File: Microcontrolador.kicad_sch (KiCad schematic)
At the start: 0 parts

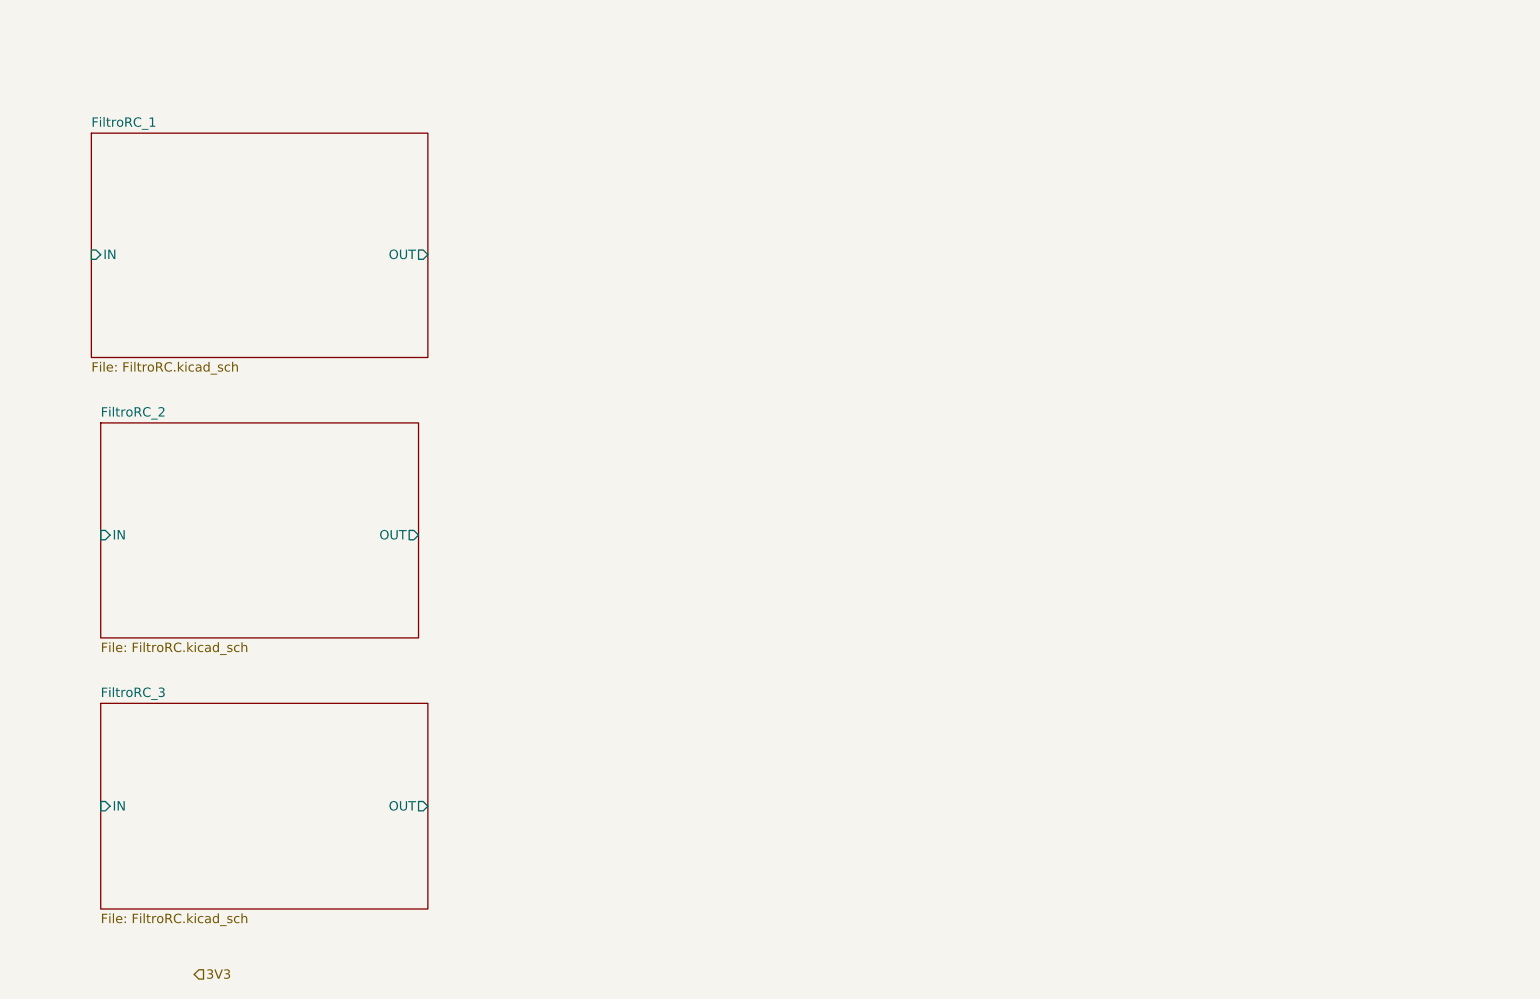
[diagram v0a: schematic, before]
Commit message: Microcontrolador: STM32G031K8T6, SWD, conector E/S y 3 filtros RC (huellas y MPN)
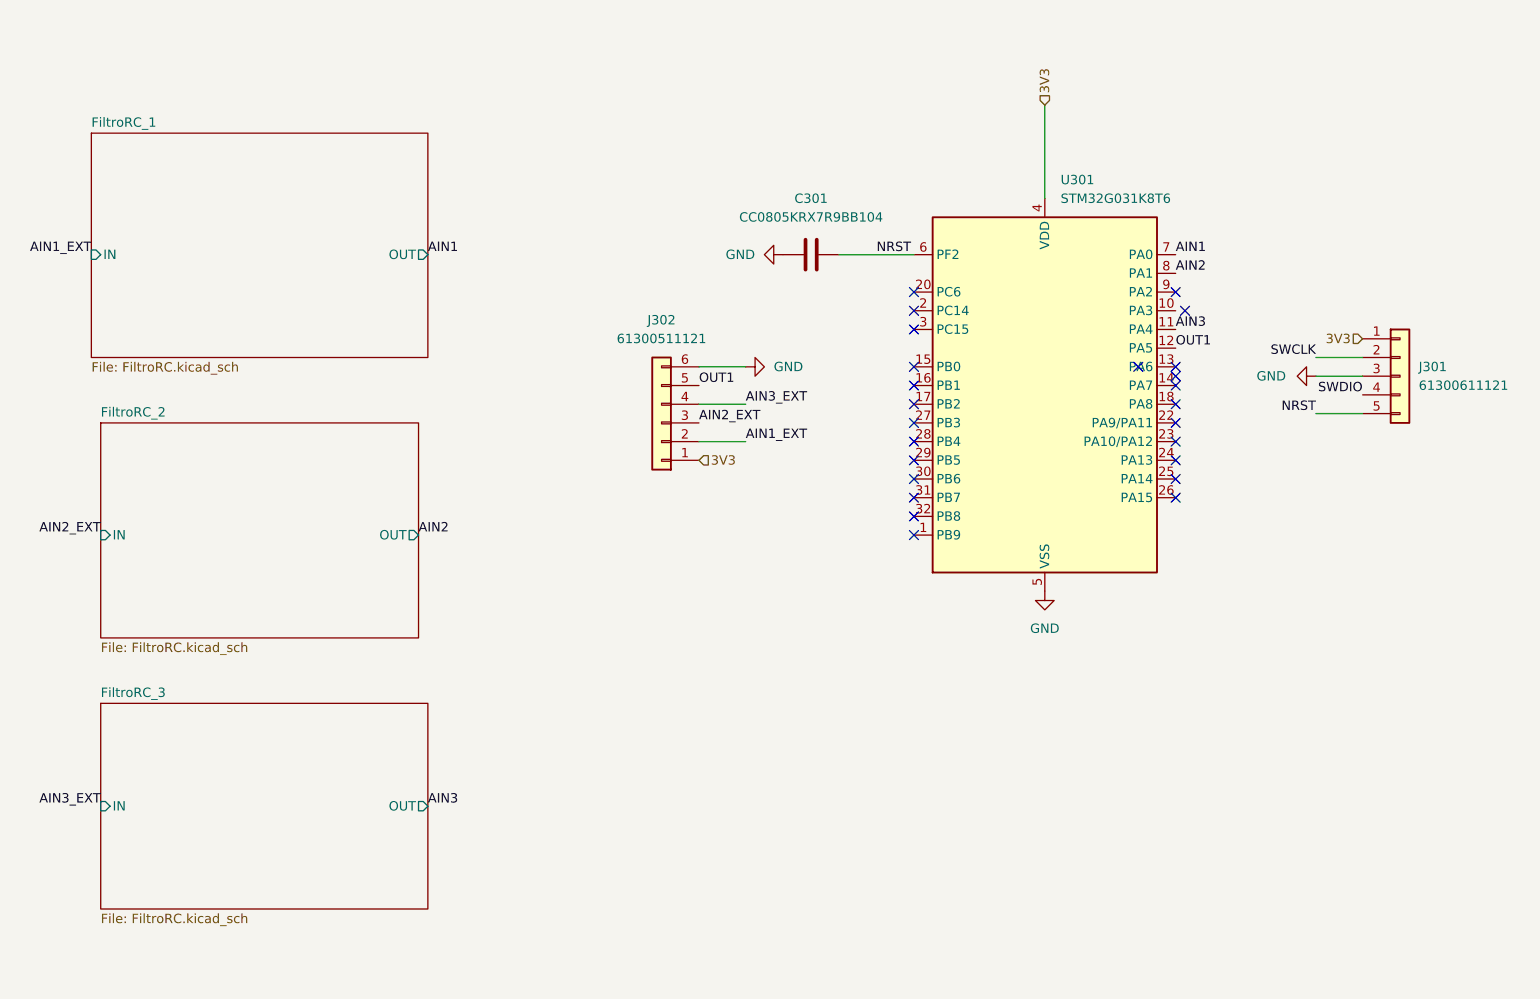
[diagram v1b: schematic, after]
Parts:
- added C301: CC0805KRX7R9BB104, Capacitor_SMD:C_0805_2012Metric_Pad1.18x1.45mm_HandSolder, symbol Device:C
- added J301: 61300611121, Connector_PinHeader_2.54mm:PinHeader_1x06_P2.54mm_Vertical, symbol Connector_Generic:Conn_01x05
- added J302: 61300511121, Connector_PinHeader_2.54mm:PinHeader_1x05_P2.54mm_Vertical, symbol Connector_Generic:Conn_01x06
- added U301: STM32G031K8T6, Package_QFP:LQFP-32_7x7mm_P0.8mm, symbol MCU_ST_STM32G0:STM32G031K8Tx
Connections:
- net 3V3: now also J301.1 (Pin_1), J302.1 (Pin_1), U301.4 (VDD)
- new net AIN1: U301.7 (PA0)
- new net AIN1_EXT: J302.2 (Pin_2)
- new net AIN2: U301.8 (PA1)
- new net AIN2_EXT: J302.3 (Pin_3)
- new net AIN3: U301.11 (PA4)
- new net AIN3_EXT: J302.4 (Pin_4)
- new net GND: C301.1, J301.3 (Pin_3), J302.6 (Pin_6), U301.5 (VSS)
- new net NRST: C301.2, J301.5 (Pin_5), U301.6 (PF2)
- new net OUT1: J302.5 (Pin_5), U301.12 (PA5)
- new net SWCLK: J301.2 (Pin_2)
- new net SWDIO: J301.4 (Pin_4)
- no-connect marks 0 -> 25

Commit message: Correcciones
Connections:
- net SWCLK: now also U301.24 (PA13)
- net SWDIO: now also U301.25 (PA14)
- no-connect marks 25 -> 23
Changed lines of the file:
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@@
+	)
+	(no_connect
+		(at 187.96 101.6)
 	)
 	(no_connect
@@
 	)
 	(no_connect
-		(at 187.96 99.06)
-	)
-	(no_connect
 		(at 187.96 83.82)
 	)
@@
 	)
 	(no_connect
-		(at 187.96 96.52)
-	)
-	(no_connect
 		(at 187.96 91.44)
 	)
@@
 	)
 	(no_connect
-		(at 187.96 101.6)
-	)
-	(no_connect
 		(at 187.96 73.66)
 	)
@@
 		(pts
 			(xy 207.01 82.55) (xy 213.36 82.55)
+		)
+		(stroke
+			(width 0)
+			(type default)
+		)
+	)
+	(wire
+		(pts
+			(xy 199.39 99.06) (xy 187.96 99.06)
+		)
+		(stroke
+			(width 0)
+			(type default)
+		)
+	)
+	(wire
+		(pts
+			(xy 187.96 96.52) (xy 191.77 96.52)
 		)
 		(stroke
@@
 		)
 	)
+	(label "SWCLK"
+		(at 191.77 96.52 0)
+		(effects
+			(font
+				(size 1.27 1.27)
+			)
+			(justify left bottom)
+		)
+	)
+	(label "SWDIO"
+		(at 199.39 99.06 0)
+		(effects
+			(font
+				(size 1.27 1.27)
+			)
+			(justify left bottom)
+		)
+	)

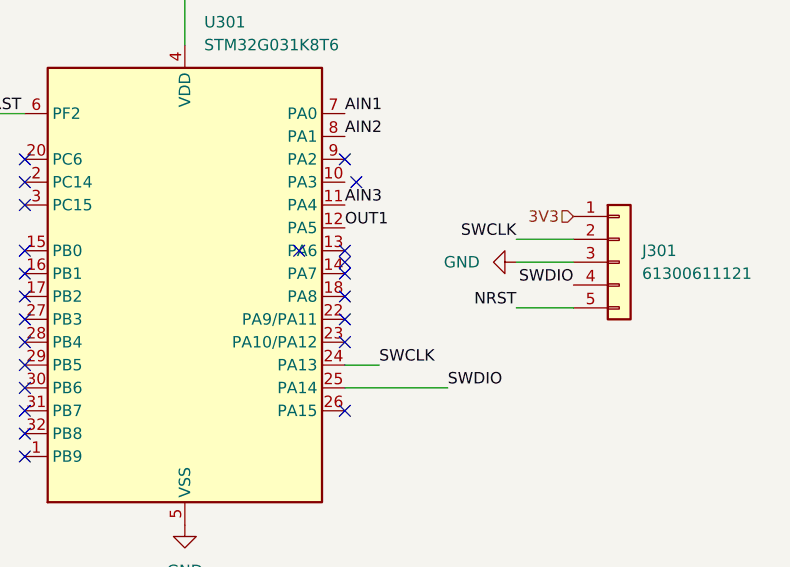
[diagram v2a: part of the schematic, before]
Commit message: Correcciones: huella C202, conectores J301/J302, SWD al MCU, MPN en su campo y BOM
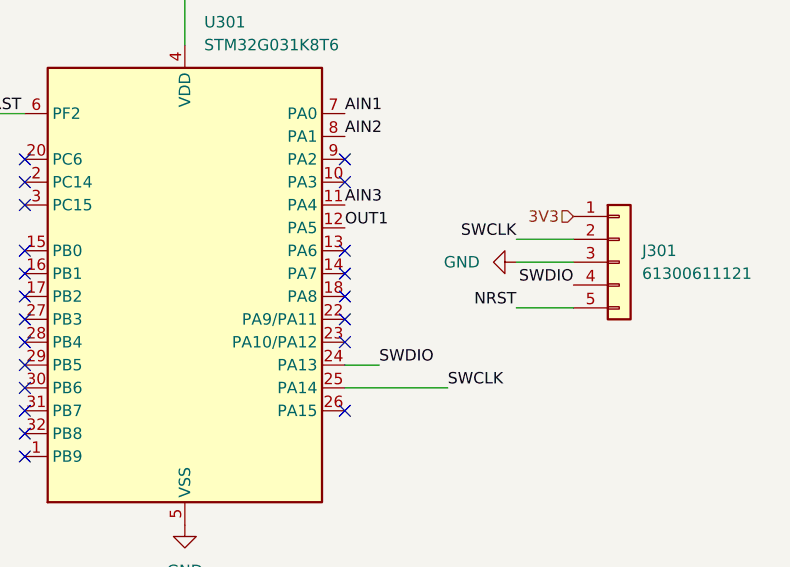
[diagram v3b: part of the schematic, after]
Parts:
- C301: MPN (none) -> CC0805KRX7R9BB104; Manufacturer (none) -> YAGEO
- J301: footprint Connector_PinHeader_2.54mm:PinHeader_1x06_P2.54mm_Vertical -> Connector_PinHeader_2.54mm:PinHeader_1x05_P2.54mm_Vertical; MPN (none) -> 61300511121; Manufacturer (none) -> Würth Elektronik
- J302: footprint Connector_PinHeader_2.54mm:PinHeader_1x05_P2.54mm_Vertical -> Connector_PinHeader_2.54mm:PinHeader_1x06_P2.54mm_Vertical; MPN (none) -> 61300611121; Manufacturer (none) -> Würth Elektronik
- U301: MPN (none) -> STM32G031K8T6; Manufacturer (none) -> STMicroelectronics
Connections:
- net SWCLK: now also U301.25 (PA14); no longer U301.24 (PA13)
- net SWDIO: now also U301.24 (PA13); no longer U301.25 (PA14)
- no-connect marks 23 -> 21
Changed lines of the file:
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@@
-	)
-	(no_connect
-		(at 182.88 83.82)
 	)
 	(no_connect
@@
 	)
 	(no_connect
-		(at 189.23 76.2)
+		(at 187.96 76.2)
 	)
 	(no_connect
@@
 	(no_connect
 		(at 187.96 83.82)
-	)
-	(no_connect
-		(at 187.96 85.09)
 	)
 	(no_connect
@@
 		)
 	)
-	(label "SWCLK"
-		(at 191.77 96.52 0)
-		(effects
-			(font
-				(size 1.27 1.27)
-			)
-			(justify left bottom)
-		)
-	)
-	(label "SWDIO"
-		(at 199.39 99.06 0)
-		(effects
-			(font
-				(size 1.27 1.27)
-			)
-			(justify left bottom)
-		)
-	)
 	(label "AIN1"
 		(at 86.36 68.58 0)
@@
 	(label "AIN3"
 		(at 187.96 78.74 0)
+		(effects
+			(font
+				(size 1.27 1.27)
+			)
+			(justify left bottom)
+		)
+	)
+	(label "SWCLK"
+		(at 199.39 99.06 0)
+		(effects
+			(font
+				(size 1.27 1.27)
+			)
+			(justify left bottom)
+		)
+	)
+	(label "SWDIO"
+		(at 191.77 96.52 0)
 		(effects
 			(font
@@
 			)
 		)
+		(property "MPN" "CC0805KRX7R9BB104"
+			(at 138.43 68.58 90)
+			(hide yes)
+			(show_name no)
+			(do_not_autoplace no)
+			(effects
+				(font
+					(size 1.27 1.27)
+				)
+			)
+		)
+		(property "Manufacturer" "YAGEO"
+			(at 138.43 68.58 90)
+			(hide yes)
+			(show_name no)
+			(do_not_autoplace no)
+			(effects
+				(font
+					(size 1.27 1.27)
+				)
+			)
+		)
 		(pin "1"
 		)
@@
 			)
 		)
+		(property "MPN" "STM32G031K8T6"
+			(at 170.18 88.9 0)
+			(hide yes)
+			(show_name no)
+			(do_not_autoplace no)
+			(effects
+				(font
+					(size 1.27 1.27)
+				)
+			)
+		)
+		(property "Manufacturer" "STMicroelectronics"
+			(at 170.18 88.9 0)
+			(hide yes)
+			(show_name no)
+			(do_not_autoplace no)
+			(effects
+				(font
+					(size 1.27 1.27)
+				)
+			)
+		)
 		(pin "12"
 		)
@@
 			)
 		)
-		(property "Footprint" "Connector_PinHeader_2.54mm:PinHeader_1x06_P2.54mm_Vertical"
+		(property "Footprint" "Connector_PinHeader_2.54mm:PinHeader_1x05_P2.54mm_Vertical"
 			(at 218.44 85.09 0)
 			(hide yes)
@@
 		)
 		(property "Description" "Generic connector, single row, 01x05, script generated (kicad-library-utils/schlib/autogen/connector/)"
+			(at 218.44 85.09 0)
+			(hide yes)
+			(show_name no)
+			(do_not_autoplace no)
+			(effects
+				(font
+					(size 1.27 1.27)
+				)
+			)
+		)
+		(property "MPN" "61300511121"
+			(at 218.44 85.09 0)
+			(hide yes)
+			(show_name no)
+			(do_not_autoplace no)
+			(effects
+				(font
+					(size 1.27 1.27)
+				)
+			)
+		)
+		(property "Manufacturer" "Würth Elektronik"
 			(at 218.44 85.09 0)
 			(hide yes)
@@
 			)
 		)
-		(property "Footprint" "Connector_PinHeader_2.54mm:PinHeader_1x05_P2.54mm_Vertical"
+		(property "Footprint" "Connector_PinHeader_2.54mm:PinHeader_1x06_P2.54mm_Vertical"
 			(at 118.11 91.44 0)
 			(hide yes)
@@
 			(at 118.11 91.44 0)
 			(hide yes)
+			(show_name no)
+			(do_not_autoplace no)
+			(effects
+				(font
+					(size 1.27 1.27)
+				)
+			)
+		)
+		(property "MPN" "61300611121"
+			(at 118.11 91.44 0)
+			(hide yes)
+			(show_name no)
+			(do_not_autoplace no)
+			(effects
+				(font
+					(size 1.27 1.27)
+				)
+			)
+		)
+		(property "Manufacturer" "Würth Elektronik"
+			(at 118.11 91.44 0)
+			(hide yes)

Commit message: Valores eléctricos en Value y BOM actualizada
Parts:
- C301: value CC0805KRX7R9BB104 -> 100n
- J301: value 61300611121 -> SWD
- J302: value 61300511121 -> E/S
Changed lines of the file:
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@@
 			)
 		)
-		(property "Value" "CC0805KRX7R9BB104"
+		(property "Value" "100n"
 			(at 138.43 63.5 90)
 			(show_name no)
@@
 			)
 		)
-		(property "Value" "61300611121"
+		(property "Value" "SWD"
 			(at 220.98 86.3599 0)
 			(show_name no)
@@
 			)
 		)
-		(property "Value" "61300511121"
+		(property "Value" "E/S"
 			(at 118.11 80.01 0)
 			(show_name no)

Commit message: Esquema: desacoplo de U301 (100 nF + 4,7 uF) y puntos de test VIN/3V3/GND
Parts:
- added C302: 4u7, Capacitor_SMD:C_0805_2012Metric_Pad1.18x1.45mm_HandSolder, symbol Device:C
- added C303: 100n, Capacitor_SMD:C_0805_2012Metric_Pad1.18x1.45mm_HandSolder, symbol Device:C
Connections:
- net 3V3: now also C302.1, C303.1
- net GND: now also C302.2, C303.2
